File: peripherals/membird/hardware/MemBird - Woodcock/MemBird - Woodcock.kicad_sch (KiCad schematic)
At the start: 15 parts, among them J1 5V, J2 5V, J3 5V, U4 74HC14, U7 AP7361EA-33E-13, Y1 Crystal

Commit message: MemBird - Woodcock Rev.1 Schematic is complete
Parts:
- removed C1, C2: 18pF, Capacitor_THT:C_Disc_D3.0mm_W2.0mm_P2.50mm, symbol Device:C_Small
- removed R1: 15k, Resistor_SMD:R_0805_2012Metric_Pad1.20x1.40mm_HandSolder, symbol Device:R
- removed U4: 74HC14, symbol 74xx:74HC14
- removed Y1: Crystal, Crystal:Crystal_HC49-4H_Vertical, symbol Device:Crystal
- added JP1: 5V / 3.3V, Jumper:SolderJumper-3_P1.3mm_Bridged12_RoundedPad1.0x1.5mm_NumberLabels, symbol Jumper:SolderJumper_3_Bridged12
- added S1: Logo_Open_Hardware_Small, Symbol:OSHW-Symbol_6.7x6mm_SilkScreen, symbol Graphic:Logo_Open_Hardware_Small
- renumbered C5 to C1, C6 to C2, J3 to J1, J1 to J2, J2 to J3, R2 to R1, U7 to U1
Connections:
- net +3.3V: now also JP1.3 (B)
- net +5V renamed VBUS
- net VBUS: now also JP1.1 (A)
- new net VMEM: JP1.2 (C)
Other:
- added sheet Logic (Logic.kicad_sch)
- note added: "3.3V REGULATOR"
- note added: "A VMEbus RAM card, for use in modular computers. - 3U P1 16-bit VME interface - 5V or 3.3V Static RAM (populate different logic chips based on RAM requirements) - 4MB maximum SRAM using 512k x 16bit chips - Supports A24 + D8O, D8E, D16 bus cycles - Does not currently support A40/MD32"
- note added: "MEMBIRD - WOODCOCK"
- note added: "MEMORY & LOGIC VOLTAGE SELECT"
- note added: "POWER TESTPOINTS"
- note removed: "MAIN CLOCK"
- note removed: "POWER"
- note removed: "POWER SUPPLY"
- moved on the sheet: C1, C2, D1, J1, J2, J3, R1, TP1, TP2, U1

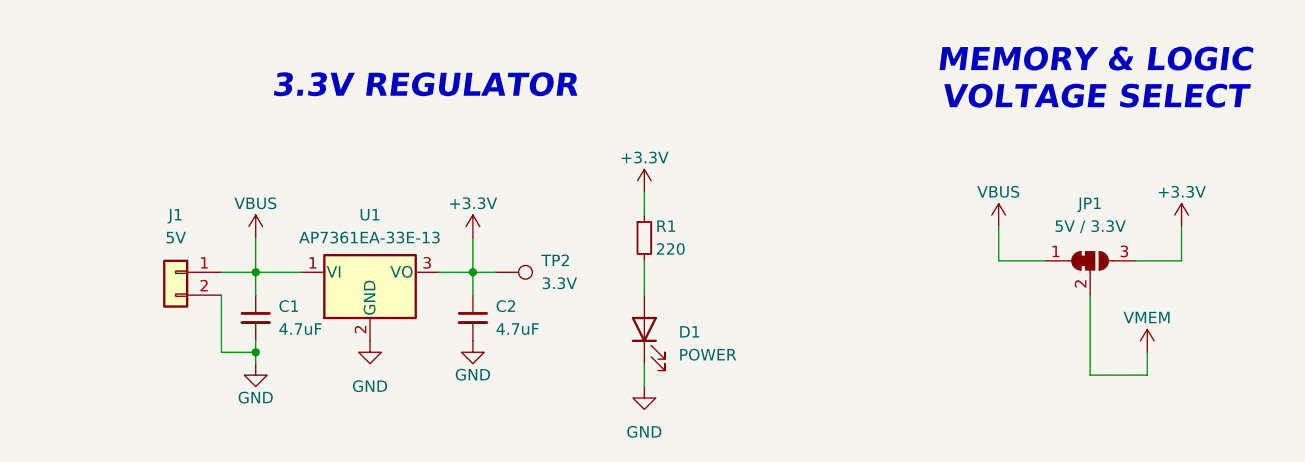
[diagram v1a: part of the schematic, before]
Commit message: Finished the MemBird - Woodcock 16-bit memory board layout
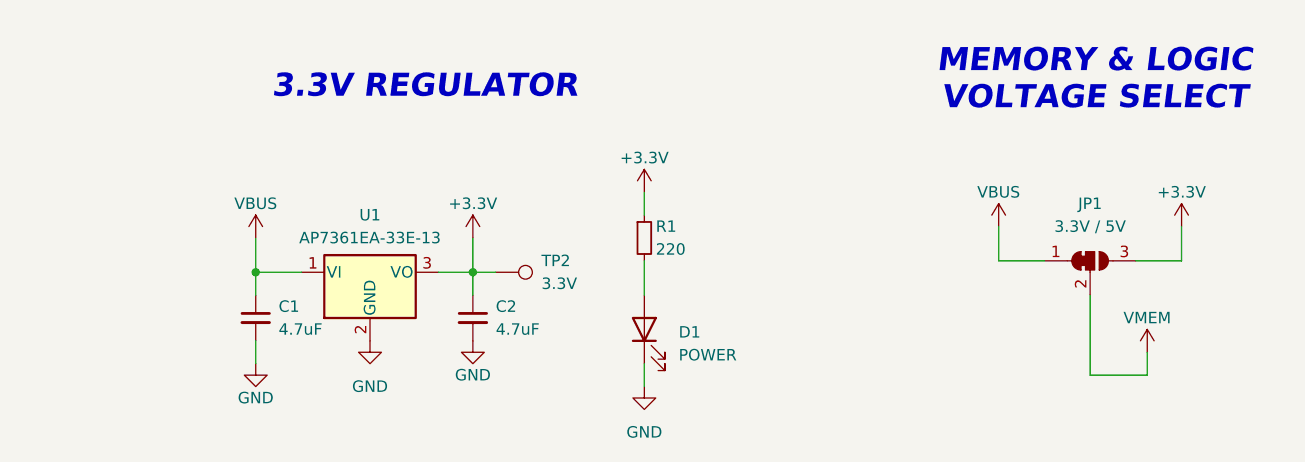
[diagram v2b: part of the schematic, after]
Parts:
- removed J1: 5V, Connector_PinHeader_2.54mm:PinHeader_1x02_P2.54mm_Vertical, symbol Connector_Generic:Conn_01x02
- JP1: value 5V / 3.3V -> 3.3V / 5V
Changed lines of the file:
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@@
-	)
-	(junction
-		(at 49.53 162.56)
-		(diameter 0)
-		(color 0 0 0 0)
 	)
 	(junction
@@
 	(wire
 		(pts
-			(xy 45.72 156.21) (xy 45.72 162.56)
-		)
-		(stroke
-			(width 0)
-			(type default)
-		)
-	)
-	(wire
-		(pts
 			(xy 132.08 152.4) (xy 137.16 152.4)
 		)
@@
 	(wire
 		(pts
-			(xy 45.72 153.67) (xy 49.53 153.67)
-		)
-		(stroke
-			(width 0)
-			(type default)
-		)
-	)
-	(wire
-		(pts
 			(xy 92.71 144.78) (xy 92.71 147.32)
 		)
@@
 	(wire
 		(pts
-			(xy 45.72 162.56) (xy 49.53 162.56)
-		)
-		(stroke
-			(width 0)
-			(type default)
-		)
-	)
-	(wire
-		(pts
 			(xy 69.85 153.67) (xy 73.66 153.67)
 		)
@@
 	(wire
 		(pts
-			(xy 49.53 162.56) (xy 49.53 163.83)
+			(xy 49.53 161.29) (xy 49.53 163.83)
 		)
 		(stroke
@@
 		(pts
 			(xy 49.53 149.86) (xy 49.53 153.67)
-		)
-		(stroke
-			(width 0)
-			(type default)
-		)
-	)
-	(wire
-		(pts
-			(xy 49.53 161.29) (xy 49.53 162.56)
 		)
 		(stroke
@@
 	)
 	(symbol
-		(lib_id "Connector_Generic:Conn_01x02")
-		(at 40.64 153.67 0)
-		(mirror y)
-		(unit 1)
-		(exclude_from_sim no)
-		(in_bom yes)
-		(on_board yes)
-		(dnp no)
-		(fields_autoplaced yes)
-		(property "Reference" "J1"
-			(at 40.64 147.32 0)
-			(effects
-				(font
-					(size 1.27 1.27)
-				)
-			)
-		)
-		(property "Value" "5V"
-			(at 40.64 149.86 0)
-			(effects
-				(font
-					(size 1.27 1.27)
-				)
-			)
-		)
-		(property "Footprint" "Connector_PinHeader_2.54mm:PinHeader_1x02_P2.54mm_Vertical"
-			(at 40.64 153.67 0)
-			(effects
-				(font
-					(size 1.27 1.27)
-				)
-				(hide yes)
-			)
-		)
-		(property "Datasheet" "~"
-			(at 40.64 153.67 0)
-			(effects
-				(font
-					(size 1.27 1.27)
-				)
-				(hide yes)
-			)
-		)
-		(property "Description" ""
-			(at 40.64 153.67 0)
-			(effects
-				(font
-					(size 1.27 1.27)
-				)
-				(hide yes)
-			)
-		)
-		(pin "1"
-		)
-		(pin "2"
-		)
-		(instances
-			(project "MemBird - Woodcock"
-				(path "/6376137f-dc27-4ca5-b911-07fd12a37fc2"
-					(reference "J1")
-					(unit 1)
-				)
-			)
-		)
-	)
-	(symbol
 		(lib_id "Device:C_Small")
 		(at 73.66 158.75 0)
@@
 			)
 		)
-		(property "Value" "5V / 3.3V"
+		(property "Value" "3.3V / 5V"
 			(at 142.24 148.59 0)
 			(effects

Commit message: k30p-VME rev.1, MemBird Woodcock rev.1, and frontpanels
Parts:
- D1: value POWER -> 3.3V POWER
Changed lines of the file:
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@@
 			)
 		)
-		(property "Value" "POWER"
+		(property "Value" "3.3V POWER"
 			(at 96.52 162.8774 90)
 			(effects
